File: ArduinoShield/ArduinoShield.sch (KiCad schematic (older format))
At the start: 41 parts, among them J1 Molex 1053131103, J2 Molex 1053131102, J3 Molex 1053131103, J4 Molex 1053131102, J5 Molex 1053131102, U1 MCP9808_DFN, U2 ALS31300, U3 BME280

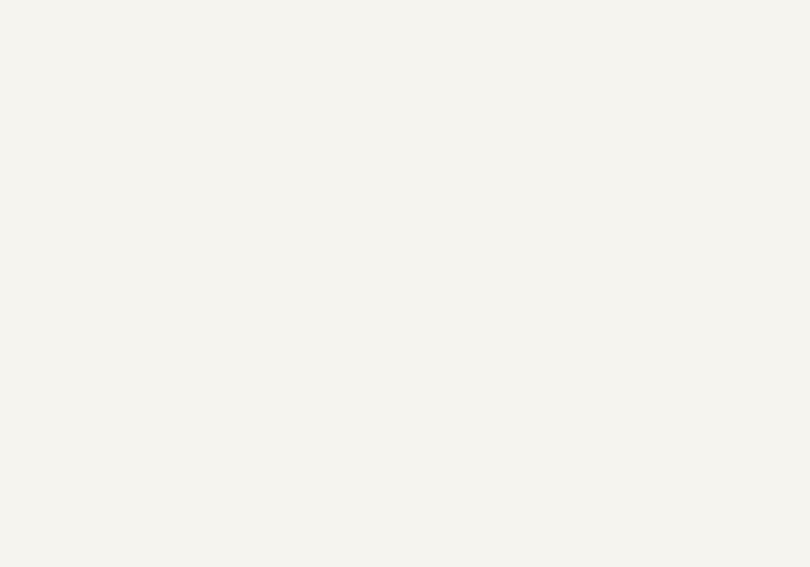
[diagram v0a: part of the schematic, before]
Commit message: Modified part that was wrong in KiCad Library (MCP9808)
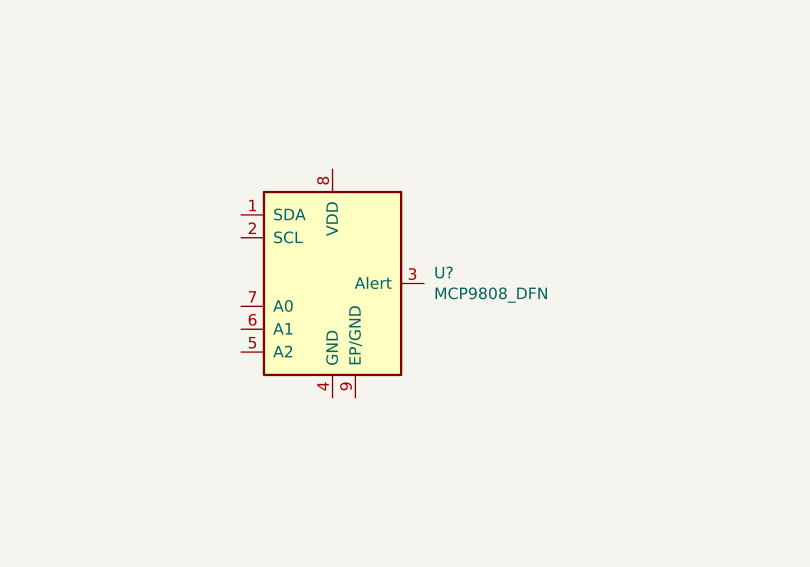
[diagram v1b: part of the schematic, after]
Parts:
- added U?: MCP9808_DFN, Package_DFN_QFN:DFN-8-1EP_3x2mm_P0.5mm_EP1.3x1.5mm, symbol ArduinoEnivronmentShield:MCP9808_DFN
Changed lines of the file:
@@
 Comment4 ""
 $EndDescr
-$Comp
-L ArduinoEnivronmentShield:MCP9808_DFN U1
-U 1 1 5E6BD66B
-P 1800 1650
-F 0 "U1" H 2244 1696 50  0000 L CNN
-F 1 "MCP9808_DFN" H 1969 1181 50  0000 L CNN
-F 2 "Package_DFN_QFN:DFN-8-1EP_3x3mm_P0.65mm_EP1.55x2.4mm" H 700 1150 50  0001 C CNN
-F 3 "http://ww1.microchip.com/downloads/en/DeviceDoc/22203b.pdf" H 1550 2100 50  0001 C CNN
-	1    1800 1650
-	1    0    0    -1
-$EndComp
 Wire Wire Line
 	1800 2150 1850 2150
@@
 	1    0    0    -1
 $EndComp
+$Comp
+L ArduinoEnivronmentShield:MCP9808_DFN U1
+U 1 1 5E6BD66B
+P 1800 1650
+F 0 "U1" H 2244 1696 50  0000 L CNN
+F 1 "MCP9808_DFN" H 1969 1181 50  0000 L CNN
+F 2 "Package_DFN_QFN:DFN-8-1EP_3x3mm_P0.65mm_EP1.55x2.4mm" H 700 1150 50  0001 C CNN
+F 3 "http://ww1.microchip.com/downloads/en/DeviceDoc/22203b.pdf" H 1550 2100 50  0001 C CNN
+	1    1800 1650
+	1    0    0    -1
+$EndComp
+$Comp
+L ArduinoEnivronmentShield:MCP9808_DFN U?
+U 1 1 5EBF3F9E
+P 6950 4350
+F 0 "U?" H 7394 4396 50  0000 L CNN
+F 1 "MCP9808_DFN" H 7394 4305 50  0000 L CNN
+F 2 "Package_DFN_QFN:DFN-8-1EP_3x2mm_P0.5mm_EP1.3x1.5mm" H 5850 3850 50  0001 C CNN
+F 3 "http://ww1.microchip.com/downloads/en/DeviceDoc/22203b.pdf" H 6700 4800 50  0001 C CNN
+	1    6950 4350
+	1    0    0    -1
+$EndComp
